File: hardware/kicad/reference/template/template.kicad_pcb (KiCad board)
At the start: 2 copper layers, 45 x 45 mm, 2 parts, among them J1 TOP, J2 BUTTOM

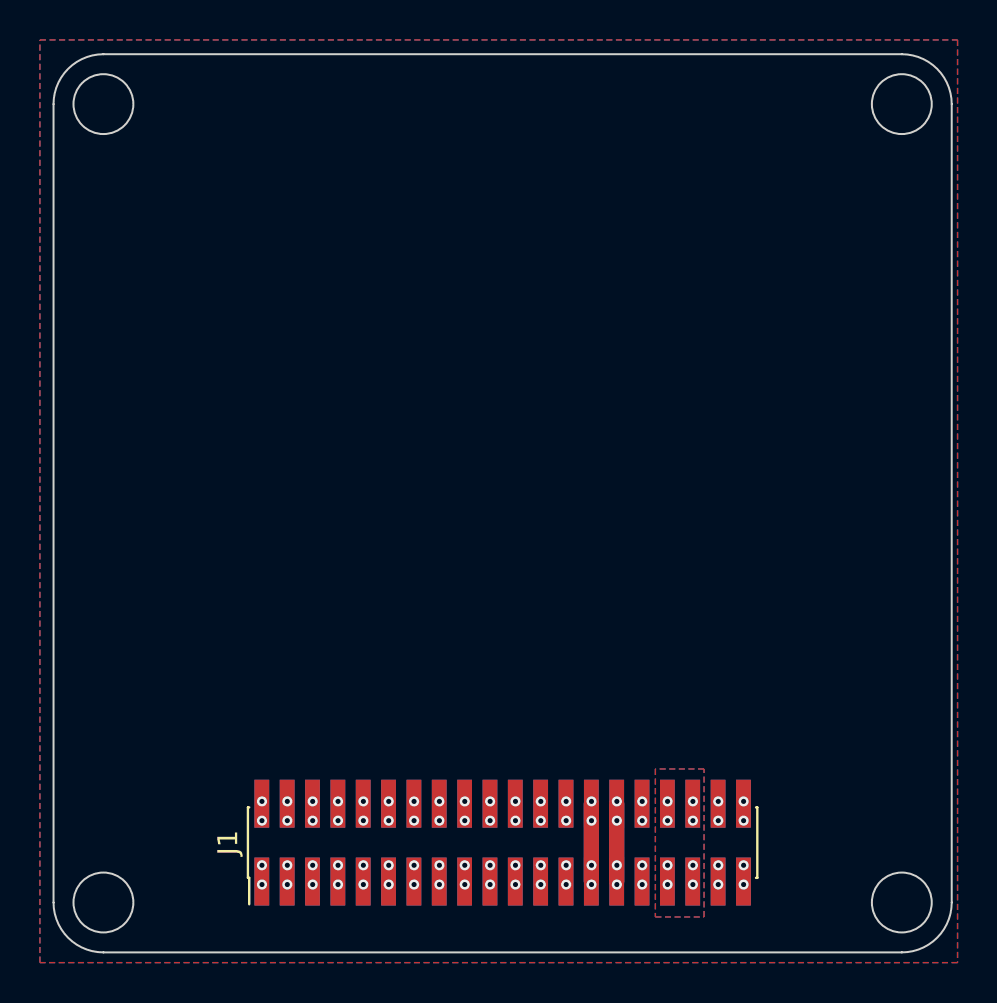
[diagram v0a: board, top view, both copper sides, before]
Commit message: 新增APP板 ADIS16460
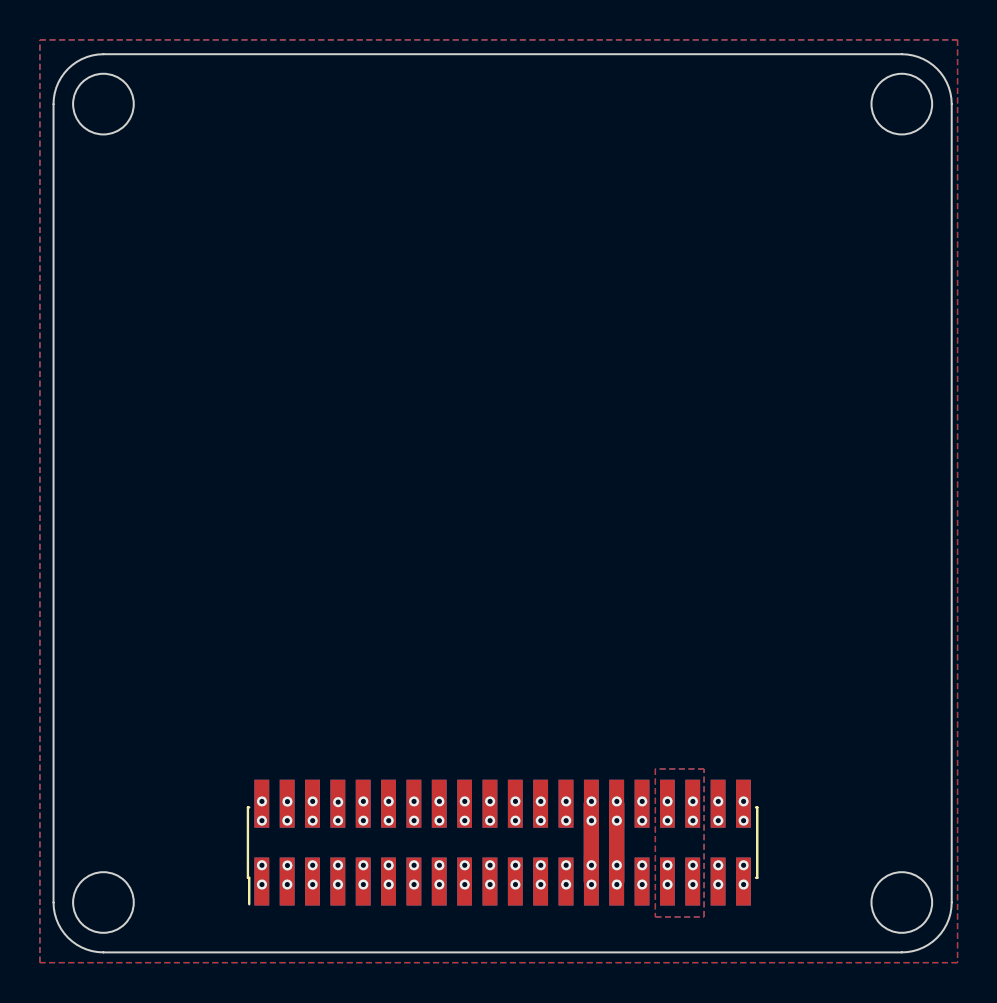
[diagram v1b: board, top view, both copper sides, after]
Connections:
- net /+3.3V renamed +3.3V
- net /+5V renamed +5V
- net /GND renamed GND
- J1 pad 10: /UART3_Tx -> /I2C_CLK
- J1 pad 11: /I2C_SDA -> /SPI_CS
- J1 pad 12: /I2C_CLK -> /SPI_CLK
- J1 pad 13: /SPI_CS -> /SPI_MOSI
- J1 pad 14: /SPI_CLK -> /SPI_MISO
- J1 pad 15: /SPI_MOSI -> /GPIO_1
- J1 pad 16: /SPI_MISO -> /GPIO_2
- J1 pad 17: /GPIO_1 -> /GPIO_3
- J1 pad 18: /GPIO_2 -> /GPIO_4
- J1 pad 19: /GPIO_3 -> /GPIO_5
- J1 pad 20: /GPIO_4 -> /GPIO_6
- J1 pad 21: /GPIO_5 -> /GPIO_7
- J1 pad 22: /GPIO_6 -> /GPIO_8
- J1 pad 23: /GPIO_7 -> /GPIO_9
- J1 pad 24: /GPIO_8 -> /GPIO_10
- J1 pad 25: /GPIO_9 -> /GPIO_11
- J1 pad 26: /GPIO_10 -> /GPIO_12
- J1 pad 9: /UART3_Rx -> /I2C_SDA
- J2 pad 10: /UART3_Rx -> /I2C_SDA
- J2 pad 11: /I2C_CLK -> /SPI_CLK
- J2 pad 12: /I2C_SDA -> /SPI_CS
- J2 pad 13: /SPI_CLK -> /SPI_MISO
- J2 pad 14: /SPI_CS -> /SPI_MOSI
- J2 pad 15: /SPI_MISO -> /GPIO_2
- J2 pad 16: /SPI_MOSI -> /GPIO_1
- J2 pad 17: /GPIO_2 -> /GPIO_4
- J2 pad 18: /GPIO_1 -> /GPIO_3
- J2 pad 19: /GPIO_4 -> /GPIO_6
- J2 pad 20: /GPIO_3 -> /GPIO_5
- J2 pad 21: /GPIO_6 -> /GPIO_8
- J2 pad 22: /GPIO_5 -> /GPIO_7
- J2 pad 23: /GPIO_8 -> /GPIO_10
- J2 pad 24: /GPIO_7 -> /GPIO_9
- J2 pad 25: /GPIO_10 -> /GPIO_12
- J2 pad 26: /GPIO_9 -> /GPIO_11
- J2 pad 9: /UART3_Tx -> /I2C_CLK
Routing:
- net /UART3_Tx: vias 2 -> 0
- net /UART3_Rx: vias 2 -> 0
- net /GPIO_12: vias 0 -> 2
- net /GPIO_11: vias 0 -> 2
